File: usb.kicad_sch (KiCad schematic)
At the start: 9 parts, among them J7 USB_C_Receptacle_USB2.0, U7 PI3USB102EZLEX

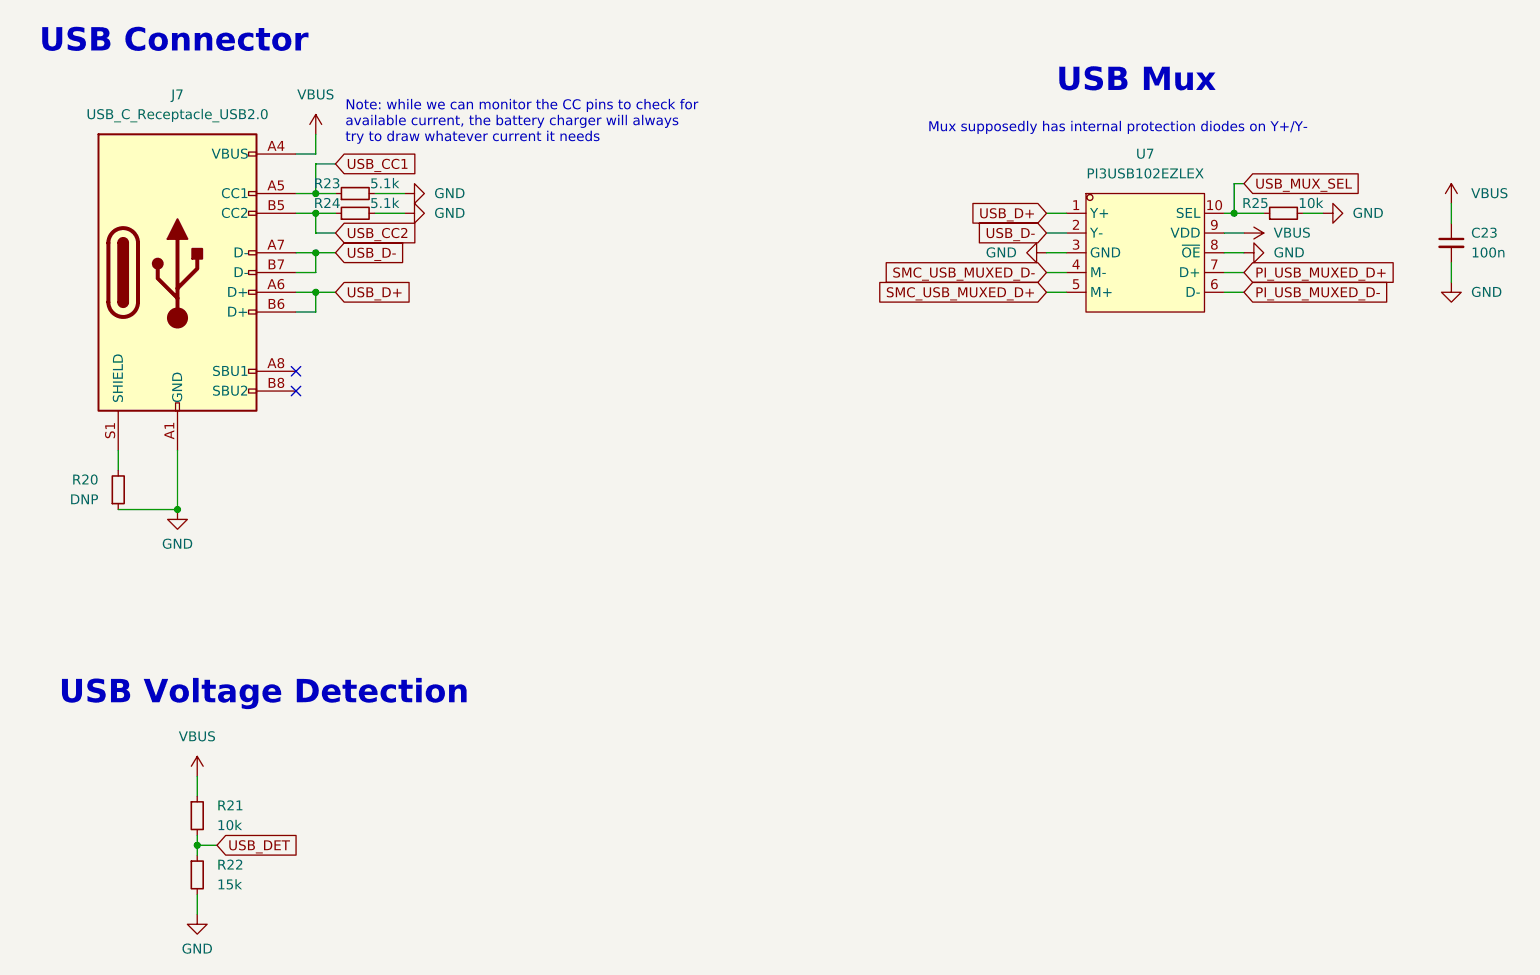
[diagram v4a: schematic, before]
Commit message: schem: migrate away from LCSC exclusive parts
- layout: migrate away from lcsc footprints
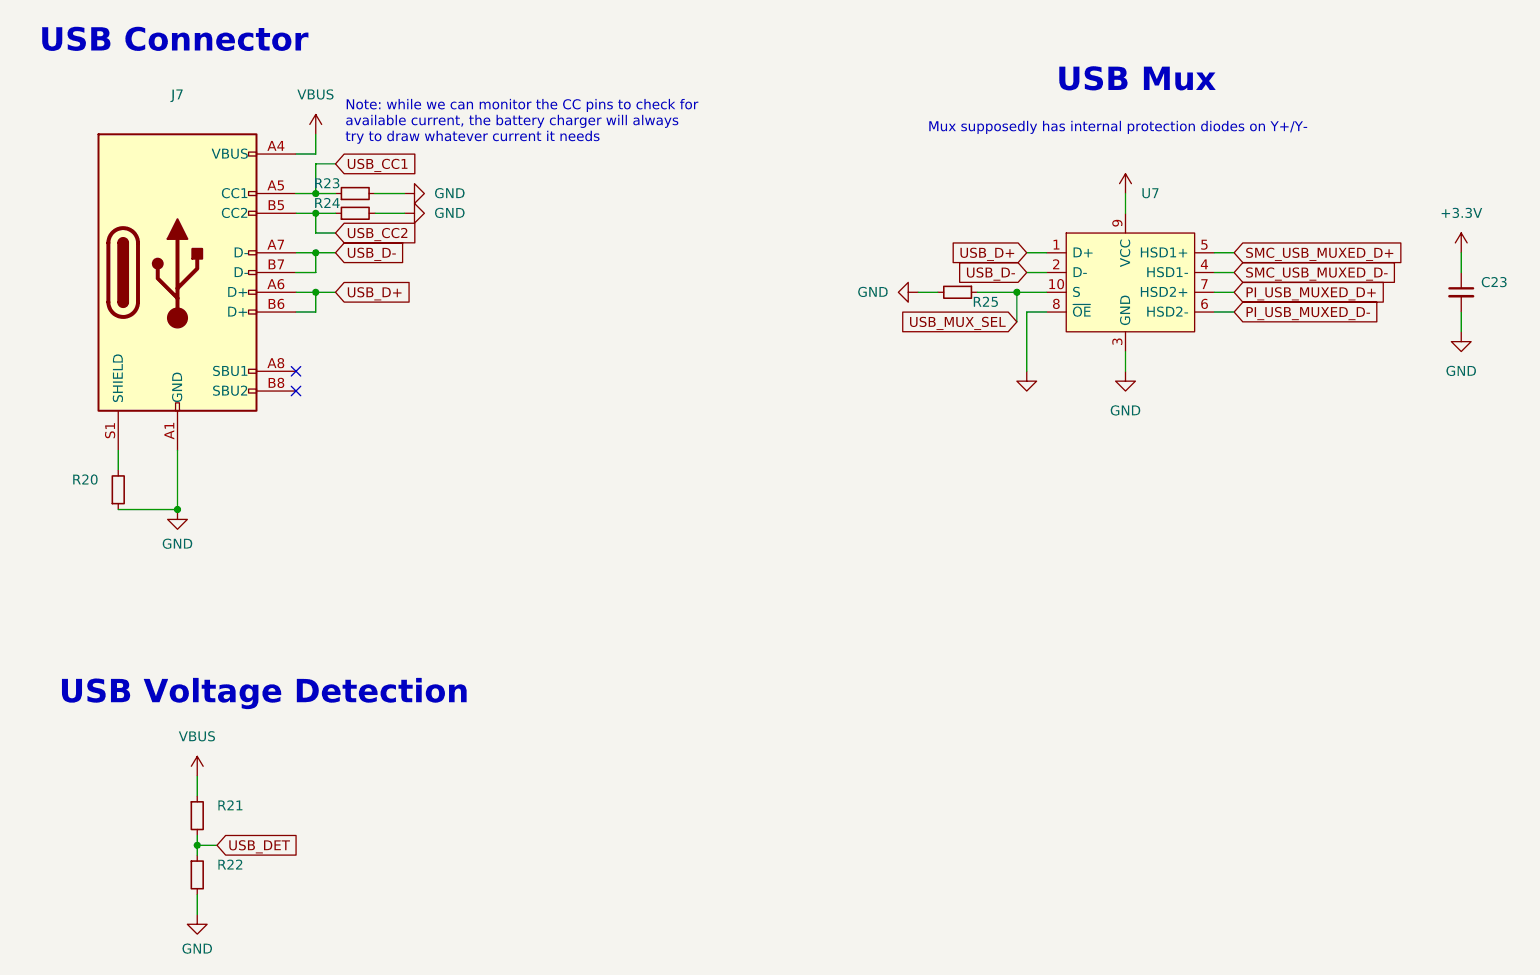
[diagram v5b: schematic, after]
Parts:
- removed U7: PI3USB102EZLEX, lcsc:TQFN-10_L1.6-W1.3-P0.50-BL, symbol lcsc:PI3USB102EZLEX
- added U7: (no value), symbol gigahawk:NLAS7242MUTBG
- C23: value 100n -> (none); footprint Capacitor_SMD:C_0402_1005Metric -> (none)
- J7: value USB_C_Receptacle_USB2.0 -> (none); footprint Gigahawk:USB_C_Receptacle_GCT_USB4085 -> (none); Digikey Part (none) -> 2073-USB4085-GF-ATR-ND; Digikey Price/Stock (none) -> https://www.digikey.com/en/products/detail/gct/USB4085-GF-A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; Manufacturer (none) -> GCT; Manufacturer Part (none) -> USB4085-GF-A; Mouser Part (none) -> 640-USB4085-GF-A; Mouser Price/Stock (none) -> https://www.mouser.ca/ProductDetail/GCT/USB4085-GF-A?qs=KUo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
- R20: value DNP -> (none); footprint Resistor_SMD:R_0402_1005Metric -> (none)
- R21, R25: value 10k -> (none); footprint Resistor_SMD:R_0402_1005Metric -> (none)
- R22: value 15k -> (none); footprint Resistor_SMD:R_0402_1005Metric -> (none)
- R23, R24: value 5.1k -> (none); footprint Resistor_SMD:R_0402_1005Metric -> (none)
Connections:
- net GND: now also U7.3 (GND), U7.8 (~{OE})
- net PI_USB_MUXED_D+: now also U7.7 (HSD2+)
- net PI_USB_MUXED_D-: now also U7.6 (HSD2-)
- net SMC_USB_MUXED_D+: now also U7.5 (HSD1+)
- net SMC_USB_MUXED_D-: now also U7.4 (HSD1-)
- net USB_D+: now also U7.1 (D+)
- net USB_D-: now also U7.2 (D-)
- net USB_MUX_SEL: now also U7.10 (S)
- net VBUS: no longer C23.1
- new net +3V3: C23.1, U7.9 (VCC)
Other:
- moved on the sheet: C23

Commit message: layout: update footprint for TP4056M
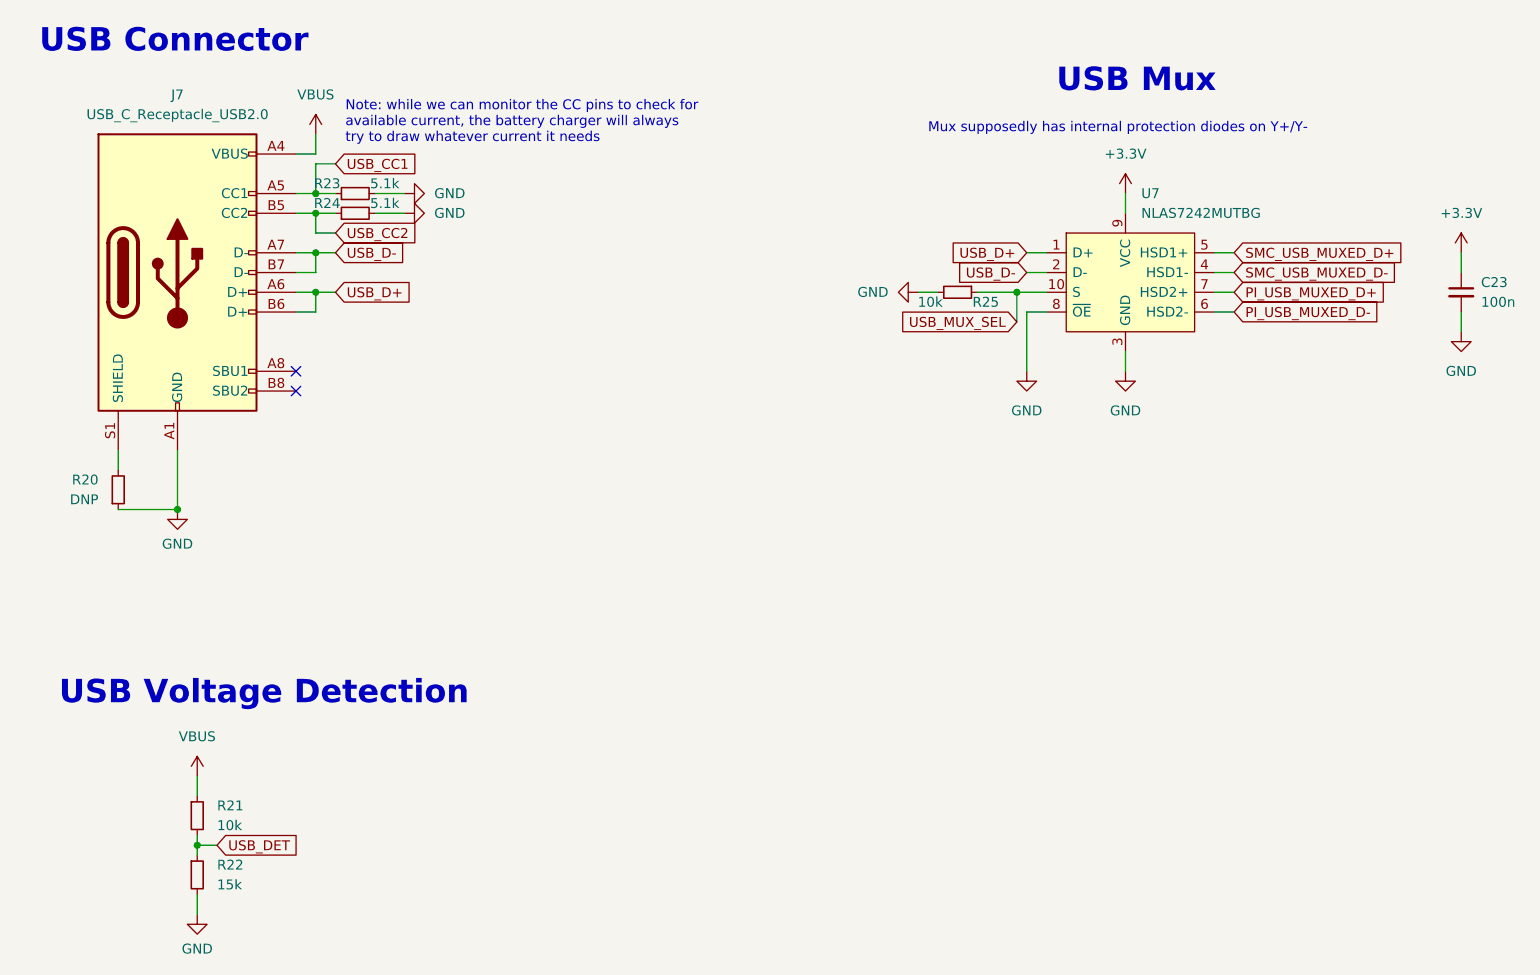
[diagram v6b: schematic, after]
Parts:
- C23: value (none) -> 100n; footprint (none) -> Capacitor_SMD:C_0402_1005Metric
- J7: value (none) -> USB_C_Receptacle_USB2.0; footprint (none) -> Gigahawk:USB_C_Receptacle_GCT_USB4085
- R20: value (none) -> DNP; footprint (none) -> Resistor_SMD:R_0402_1005Metric
- R21, R25: value (none) -> 10k; footprint (none) -> Resistor_SMD:R_0402_1005Metric
- R22: value (none) -> 15k; footprint (none) -> Resistor_SMD:R_0402_1005Metric
- R23, R24: value (none) -> 5.1k; footprint (none) -> Resistor_SMD:R_0402_1005Metric
- U7: value (none) -> NLAS7242MUTBG; footprint (none) -> Package_DFN_QFN:UQFN-10_1.4x1.8mm_P0.4mm
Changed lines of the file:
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@@
       (effects (font (size 1.27 1.27)) (justify left))
     )
-    (property "Value" "" (id 1) (at 68.58 158.7499 0)
-      (effects (font (size 1.27 1.27)) (justify left))
-    )
-    (property "Footprint" "" (id 2) (at 66.04 157.48 0)
+    (property "Value" "15k" (id 1) (at 68.58 158.7499 0)
+      (effects (font (size 1.27 1.27)) (justify left))
+    )
+    (property "Footprint" "Resistor_SMD:R_0402_1005Metric" (id 2) (at 66.04 157.48 0)
       (effects (font (size 1.27 1.27)) hide)
     )
@@
       (effects (font (size 1.27 1.27)) (justify left))
     )
-    (property "Value" "" (id 1) (at 161.925 83.82 90)
-      (effects (font (size 1.27 1.27)) (justify right))
-    )
-    (property "Footprint" "" (id 2) (at 163.83 82.55 0)
+    (property "Value" "10k" (id 1) (at 161.925 83.82 90)
+      (effects (font (size 1.27 1.27)) (justify right))
+    )
+    (property "Footprint" "Resistor_SMD:R_0402_1005Metric" (id 2) (at 163.83 82.55 0)
       (effects (font (size 1.27 1.27)) hide)
     )
@@
       (effects (font (size 1.27 1.27)) (justify left))
     )
-    (property "Value" "" (id 1) (at 68.58 151.1299 0)
-      (effects (font (size 1.27 1.27)) (justify left))
-    )
-    (property "Footprint" "" (id 2) (at 66.04 149.86 0)
+    (property "Value" "10k" (id 1) (at 68.58 151.1299 0)
+      (effects (font (size 1.27 1.27)) (justify left))
+    )
+    (property "Footprint" "Resistor_SMD:R_0402_1005Metric" (id 2) (at 66.04 149.86 0)
       (effects (font (size 1.27 1.27)) hide)
     )
@@
       (effects (font (size 1.27 1.27)) (justify left))
     )
-    (property "Value" "" (id 1) (at 88.265 68.58 90)
-      (effects (font (size 1.27 1.27)) (justify right))
-    )
-    (property "Footprint" "" (id 2) (at 86.36 69.85 0)
+    (property "Value" "5.1k" (id 1) (at 88.265 68.58 90)
+      (effects (font (size 1.27 1.27)) (justify right))
+    )
+    (property "Footprint" "Resistor_SMD:R_0402_1005Metric" (id 2) (at 86.36 69.85 0)
       (effects (font (size 1.27 1.27)) hide)
     )
@@
       (effects (font (size 1.27 1.27)) (justify left))
     )
-    (property "Value" "" (id 1) (at 187.4394 72.39 0)
-      (effects (font (size 1.27 1.27)) (justify left))
-    )
-    (property "Footprint" "" (id 2) (at 167.64 64.77 0)
+    (property "Value" "NLAS7242MUTBG" (id 1) (at 187.4394 72.39 0)
+      (effects (font (size 1.27 1.27)) (justify left))
+    )
+    (property "Footprint" "Package_DFN_QFN:UQFN-10_1.4x1.8mm_P0.4mm" (id 2) (at 167.64 64.77 0)
       (effects (font (size 1.27 1.27)) (justify left) hide)
     )
@@
       (effects (font (size 1.27 1.27)) (justify left))
     )
-    (property "Value" "" (id 1) (at 231.14 83.8262 0)
-      (effects (font (size 1.27 1.27)) (justify left))
-    )
-    (property "Footprint" "" (id 2) (at 228.6 82.55 0)
+    (property "Value" "100n" (id 1) (at 231.14 83.8262 0)
+      (effects (font (size 1.27 1.27)) (justify left))
+    )
+    (property "Footprint" "Capacitor_SMD:C_0402_1005Metric" (id 2) (at 228.6 82.55 0)
       (effects (font (size 1.27 1.27)) hide)
     )
@@
       (effects (font (size 1.27 1.27)) hide)
     )
-    (property "Value" "" (id 1) (at 172.72 97.79 0))
+    (property "Value" "GND" (id 1) (at 172.72 97.79 0))
     (property "Footprint" "" (id 2) (at 172.72 92.71 0)
       (effects (font (size 1.27 1.27)) hide)
@@
       (effects (font (size 1.27 1.27)) (justify left))
     )
-    (property "Value" "" (id 1) (at 88.265 71.12 90)
-      (effects (font (size 1.27 1.27)) (justify right))
-    )
-    (property "Footprint" "" (id 2) (at 86.36 72.39 0)
+    (property "Value" "5.1k" (id 1) (at 88.265 71.12 90)
+      (effects (font (size 1.27 1.27)) (justify right))
+    )
+    (property "Footprint" "Resistor_SMD:R_0402_1005Metric" (id 2) (at 86.36 72.39 0)
       (effects (font (size 1.27 1.27)) hide)
     )
@@
     (in_bom yes) (on_board yes) (fields_autoplaced)
     (property "Reference" "J7" (id 0) (at 63.5 57.15 0))
-    (property "Value" "" (id 1) (at 63.5 59.69 0))
-    (property "Footprint" "" (id 2) (at 67.31 80.01 0)
+    (property "Value" "USB_C_Receptacle_USB2.0" (id 1) (at 63.5 59.69 0))
+    (property "Footprint" "Gigahawk:USB_C_Receptacle_GCT_USB4085" (id 2) (at 67.31 80.01 0)
       (effects (font (size 1.27 1.27)) hide)
     )
@@
       (effects (font (size 1.27 1.27)) hide)
     )
-    (property "Value" "" (id 1) (at 185.42 64.77 0))
+    (property "Value" "+3.3V" (id 1) (at 185.42 64.77 0))
     (property "Footprint" "" (id 2) (at 185.42 69.85 0)
       (effects (font (size 1.27 1.27)) hide)
@@
       (effects (font (size 1.27 1.27)) (justify right))
     )
-    (property "Value" "" (id 1) (at 53.34 109.2199 0)
-      (effects (font (size 1.27 1.27)) (justify right))
-    )
-    (property "Footprint" "" (id 2) (at 55.88 107.95 0)
-      (effects (font (size 1.27 1.27)) hide)
-    )
+    (property "Value" "DNP" (id 1) (at 53.34 109.2199 0)
+      (effects (font (size 1.27 1.27)) (justify right))
+    )
+    (property "Footprint" "Resistor_SMD:R_0402_1005Metric" (id 2) (at 55.88 107.95 0)
+      (effects (font (size 1.27 1.27)) hide)
+    )
